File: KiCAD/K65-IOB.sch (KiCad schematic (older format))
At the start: 24 parts, among them J1 SBC6303 BUS, J2 PIO-A, J3 Conn_01x06, J4 PIO-B, U1 74HC139, U2 74HC04, U3 74HC74, U4 74HC125, U5 W65C51, U6 W65C22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

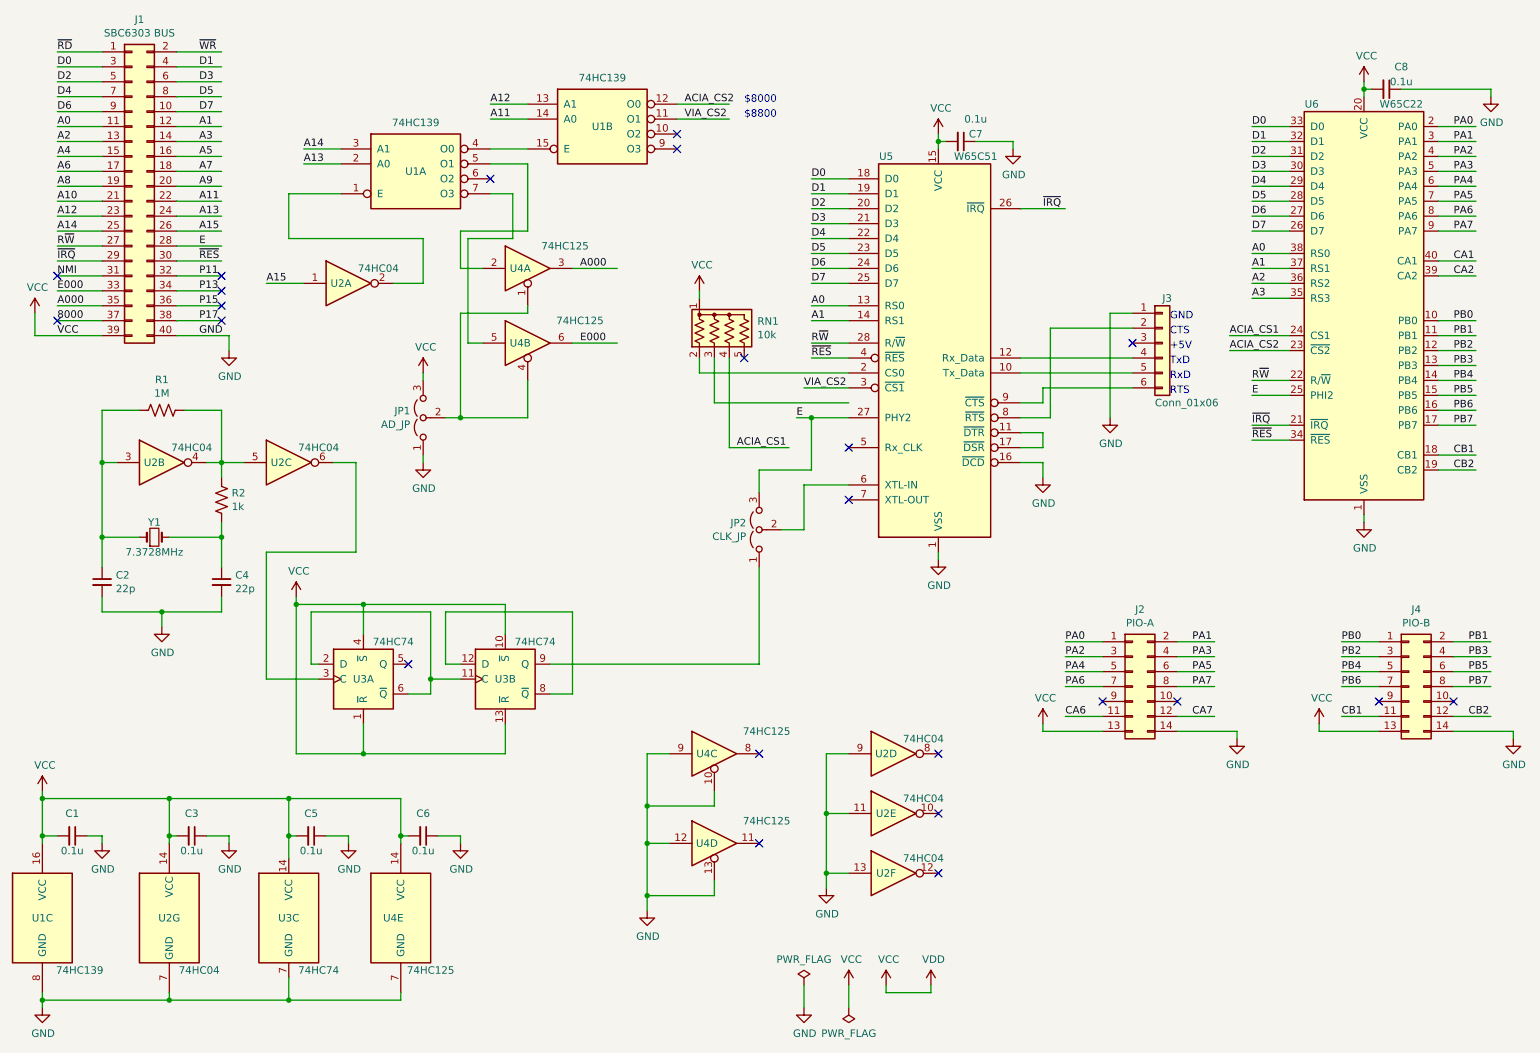
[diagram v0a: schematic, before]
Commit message: アドレスデコーダーを簡易版へ
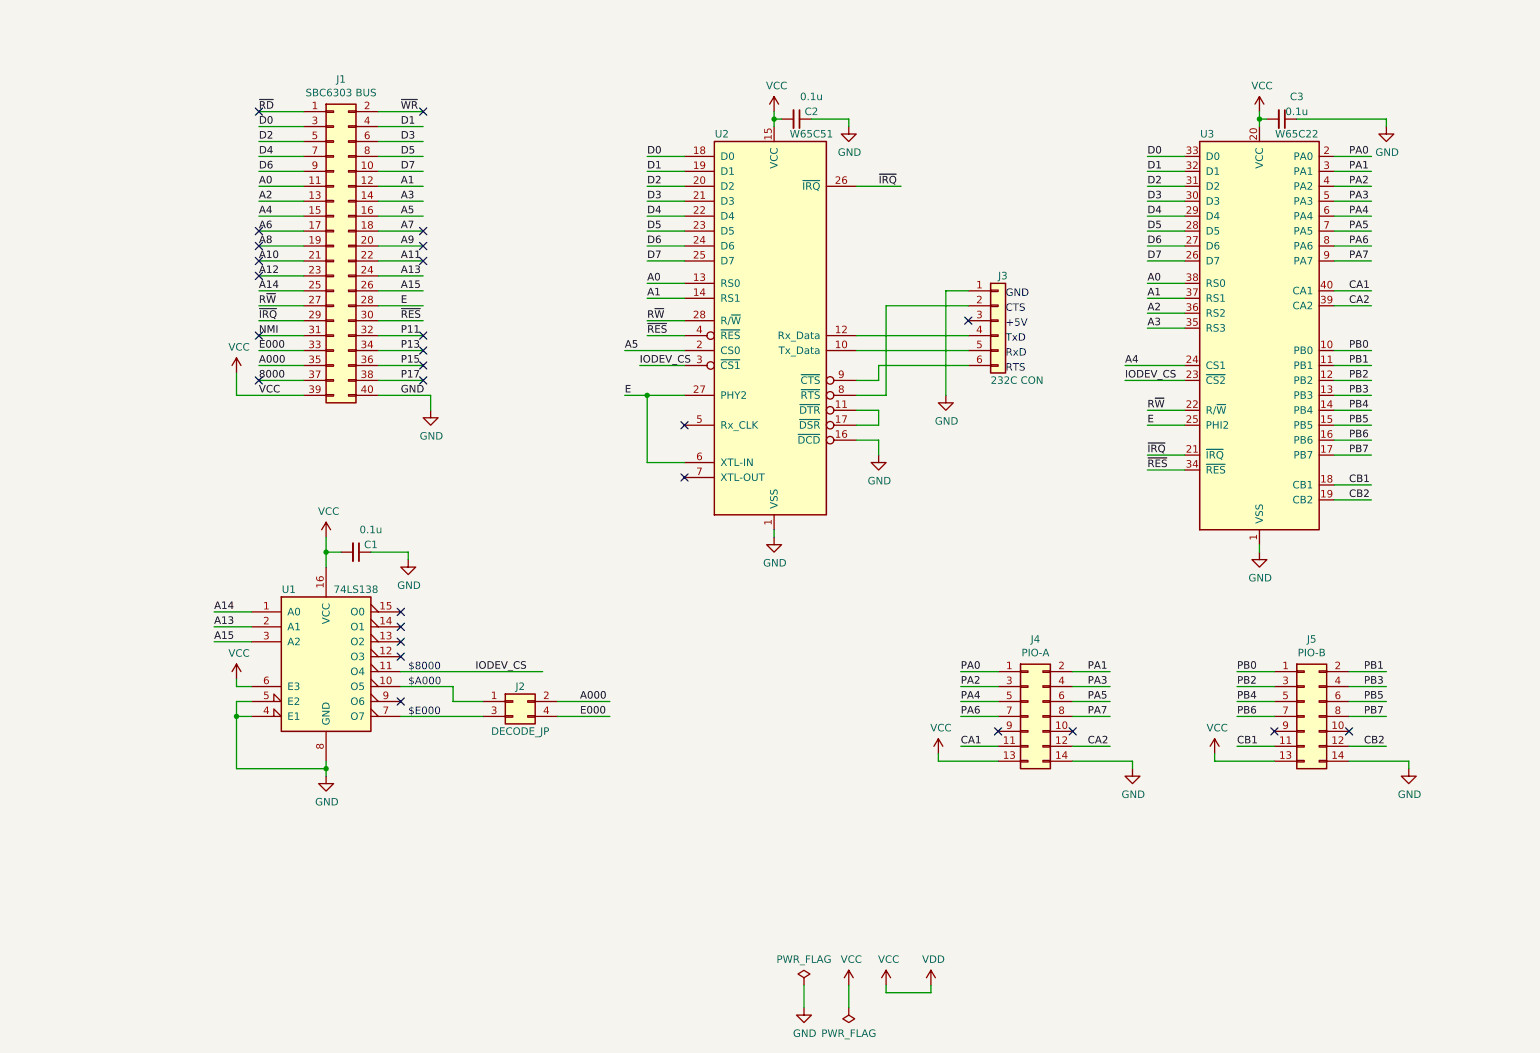
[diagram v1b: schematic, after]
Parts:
- removed C2, C4: 22p, symbol Device:C_Small
- removed C3, C5, C6: 0.1u, symbol Device:C_Small
- removed JP1: AD_JP, symbol Jumper:Jumper_3_Open
- removed JP2: CLK_JP, symbol Jumper:Jumper_3_Open
- removed R1: 1M, symbol Device:R_US
- removed R2: 1k, symbol Device:R_US
- removed RN1: 10k, Resistor_THT:R_Array_SIP5, symbol Device:R_Network04_US
- removed U1: 74HC139, symbol 74xx:74LS139
- removed U2: 74HC04, symbol 74xx:74HC04
- removed U3: 74HC74, symbol 74xx:74HC74
- removed U4: 74HC125, symbol 74xx:74LS125
- removed Y1: 7.3728MHz, symbol Device:Crystal_Small
- added J2: DECODE_JP, symbol Connector_Generic:Conn_02x02_Odd_Even
- added U1: 74LS138, symbol 74xx:74LS138
- J3: value Conn_01x06 -> 232C CON
- renumbered C7 to C2, C8 to C3, J2 to J4, J4 to J5, U5 to U2, U6 to U3
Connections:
- net labels added: IODEV_CS
- net labels removed: ACIA_CS1, ACIA_CS2, CA6, CA7, VIA_CS2
- wire segments 298 -> 183
- no-connect marks 23 -> 27
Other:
- note added: "$A000"
- note added: "$E000"
- note removed: "$8800"
- moved on the sheet: C2, C3, J1, J3, J4, J5, U2, U3

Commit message: VIA/ACIAアドレス表示追加
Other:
- note added: "ACIA : $8020-8023"
- note added: "VIA : $8010-801F"
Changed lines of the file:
@@
 NoConn ~ 3450 2350
 NoConn ~ 3450 2450
+Text Notes 6000 4250 0    50   ~ 0
+ACIA : $8020-8023
+Text Notes 9300 4350 0    50   ~ 0
+VIA : $8010-801F
 $EndSCHEMATC
